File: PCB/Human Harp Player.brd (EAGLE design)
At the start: 70 x 70 mm, 41 parts, among them J1 4UCON 20404, J3 Sparkfun: PRT-00553, J4 Sparkfun: PRT-00553, J5 Sparkfun: PRT-00553, J6 Sparkfun: PRT-00553, J7 ICSP, J8 Molex: 500075-1517, Q1 MMBT2222A, Q3 STD26P3LLH6, U1 DSPIC33EP512GM604-I/PT, U2 MIC5319-3.3YD5, U3 Sparkfun: PRT-00116, X1 ABM8-16.000MHZ-B2-T

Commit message: Commit PCB Rev. 2
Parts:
- removed J6: Sparkfun: PRT-00553, SparkFun:1X06
- removed J7: ICSP, SparkFun-Connectors:1X06_NO_SILK
- removed J8: Molex: 500075-1517, x-io:500075-1517
- removed LED1: Sparkfun: COM-12903 (purple), SparkFun-LED:LED5MM
- removed Q3: STD26P3LLH6, transistor-fet:TO252
- removed R10: 10k, 0603, SparkFun:0402-RES
- removed R11: 15R, 0603, SparkFun:0402-RES
- removed S1: RS: 5MS1S102AM2QES, x-io:5MS1S102AM2QES
- removed S2: TE Connectivity: FSM4JAH, SparkFun-Electromechanical:TACTILE-PTH
- removed U$3: (no value), x-io:HUMAN_HARP_LOGO_20MM_BOTTOM
- added C12, C15, C16: 100n, 0603, SparkFun:0402-CAP
- added C13, C14: 22p, 0603, SparkFun:0402-CAP
- added J2: Unpopulated, SparkFun-Connectors:1X05
- added L1: 220u, 510mA, EATON-DRA73-221-R, rcl:PIS2816
- added LOGO1: OSHW-LOGOL, SparkFun-Aesthetics:OSHW-LOGO-L
- added Q2: IRLML6401PBF, SparkFun-DiscreteSemi:SOT23-3
- added U$2: (no value), x-io:HEDS-5600-A06
- added U4: DSPIC33EP512GM604-I/PT, x-io:TQFP44
- added U5, U6: WS2811, SparkFun-LED:LED-TRICOLOR-5050-IC
- C1: value 100n, 0603 -> 470u, 16V, Pansonic F; device SparkFun:0402-CAP -> rcl:PANASONIC_F
- C10, C8: value 100n, 0603 -> 10u, 0603
- C11: value 470u, 10V, Tant, Case E -> 10u, 0603; device rcl:SMC_E -> SparkFun:0402-CAP
- C5, C6: value 22p, 0603 -> 100n, 0603
- C9: value 10u, 0603 -> 100n, 0603
- J1: value 4UCON 20404 -> Sparkfun-PRT-00587; device x-io:JST-R/A -> SparkFun-Connectors:USB-MINIB
- J3: value Sparkfun: PRT-00553 -> Sparkfun: PRT-00116
- J4: value Sparkfun: PRT-00553 -> Unpopulated; device SparkFun-Connectors:1X05 -> SparkFun-Connectors:1X06_NO_SILK
- J5: value Sparkfun: PRT-00553 -> Sparkfun: PRT-00116; device SparkFun-Connectors:1X03 -> SparkFun-Connectors:1X05
- Q1: value MMBT2222A -> IRLML6401PBF
- R1, R6, R7: value 10k 0603 -> 4k7, 0603
- R2, R3, R4, R5, R8, R9: value 10k, 0603 -> 4k7, 0603
- U$1: device x-io:X-IO_TECHNOLOGIES_LOGO_10MM_BOTTOM -> x-io:X-IO_TECHNOLOGIES_LOGO_10MM_TOP
- U$4: value OSHW_LOGO6MM_BOTTOM -> (none); device x-io:OSHW_LOGO_6MM_BOTTOM -> x-io:HUMAN_HARP_LOGO_20MM_TOP
- U1: value DSPIC33EP512GM604-I/PT -> FT232RL; device x-io:TQFP44 -> SparkFun:SSOP28DB
- U2: value MIC5319-3.3YD5 -> BMX055; device x-io:SOT23-5 -> x-io:BMX055
- U3: value Sparkfun: PRT-00116 -> MIC5319-3.3YD5; device x-io-EAGLE-Library:X-OSC_TH -> x-io:SOT23-5
- X1: value ABM8-16.000MHZ-B2-T -> ABRACON-ABM8-16.000MHZ-B2-T
- moved J1 56.9 mm to (32.4, 66.0), turned to 180 degrees
- moved R8 45.2 mm to (63.5, 15.2), flipped to the top, turned to 180 degrees
- moved Q1 45.0 mm to (14.0, 55.9), flipped to the top, turned to 270 degrees
- moved C11 44.3 mm to (12.7, 31.1), flipped to the top, turned to 0 degrees
- moved C8 43.9 mm to (26.7, 55.9), flipped to the top, turned to 270 degrees
- moved C10 43.5 mm to (33.0, 55.9), flipped to the top
- moved R6 40.2 mm to (24.1, 54.6), flipped to the top
- moved R3 40.0 mm to (55.9, 15.2), flipped to the top, turned to 180 degrees
- moved C2 37.8 mm to (15.2, 62.2), flipped to the top, turned to 90 degrees
- moved J5 37.7 mm to (63.5, 27.9)
- moved R7 36.4 mm to (21.6, 54.6), flipped to the top
- moved J3 33.8 mm to (55.9, 27.9), turned to 270 degrees
- moved R4 33.7 mm to (55.9, 13.3), flipped to the top, turned to 180 degrees
- moved C9 33.6 mm to (26.7, 52.1), flipped to the top, turned to 270 degrees
- moved U2 31.6 mm to (37.5, 41.9), flipped to the top, turned to 0 degrees
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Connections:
- removed net AUX: J7.6, U1.25
- removed net BATTERY_LEVEL: C10.1, R6.1, R7.2, U1.19
- removed net BUTTON: S2.3, U1.26
- removed net ENCODER_VDD: J3.2, R2.2, R3.2, U1.35
- removed net IMU_INT: J4.4, U1.36
- removed net IMU_SCL: J4.3, R4.1, U1.38
- removed net IMU_SDA: J4.1, R5.1, U1.37
- removed net IMU_VDD: J4.2, R4.2, R5.2, U1.41
- removed net IN1: J6.2, U1.44, U3.1
- removed net LED: R11.1, U1.34
- removed net OUT1: J6.3, U1.43, U3.36
- removed net OUT16: J5.3, U3.21
- removed net POWER_ENABLE: U1.1
- removed net VIN: C11.+, C7.1, Q3.2, R6.2, R9.2, S1.2, U2.1, U2.3
- removed net X-OSC_ENABLE: R10.2, R8.1
- removed net X-OSC_PWR: J5.2, Q3.3, U3.20
- new net 3V3: C10.1, C12.1, C15.1, C16.2, R5.1, U3.5, U4.17, U4.28, U4.40
- new net 5V: C8.1, J3.2, Q1.3, R3.2, R4.2, U3.1, U3.3, U5.3, U5.5, U6.3, U6.5
- new net BMX055_INT: J2.4, J5.4, U2.14, U4.36
- new net BMX055_SCL: J2.3, J5.3, R8.1, U2.9, U4.38
- new net BMX055_SDA: J2.1, J5.1, R9.1, U2.11, U4.37
- new net FTDI_D+: J1.D+, U1.15
- new net FTDI_D-: J1.D-, U1.16
- new net FTDI_RX: R6.1, U1.5
- new net FTDI_SLEEP: Q2.1, R1.2, U1.12
- new net FTDI_TX: R7.1, U1.1
- new net N$6: J1.VBUS, L1.1
- new net N$8: U5.1, U6.2
- new net TEST: J4.6, U4.25
- new net VSENSORS: C5.1, C6.1, C7.2, J2.2, J5.2, R8.2, R9.2, U2.13, U2.3, U2.7, U4.41
- new net WS2811_DATA: U4.2, U5.2
- net ENCODER_A: now also R3.1, U4.32; no longer R2.1, U1.32
- net ENCODER_B: now also R4.1, U4.33; no longer R3.1, U1.33
- net GND: now also C1.-, C11.2, C12.2, C13.1, C14.1, C15.2, C16.1, C2.1, C3.1, C7.1, J1.GND, J2.5, J4.3, J5.5, R1.1, R2.1, U1.11, U1.18, U1.21, U1.25, U1.26, U1.7, U2.12, U2.17, U2.20, U2.4, U2.6, U3.2, U4.16, U4.29, U4.39, U4.6, U5.6, U6.6; no longer C1.2, C11.-, C2.2, C3.2, C7.2, J1.-, J4.5, J5.1, J6.5, J6.6, J7.3, J8.GND, LED1.K, Q1.2, R7.1, S2.1, U1.16, U1.29, U1.39, U1.6, U2.2, U3.19
- net MCLR: now also J4.1, R5.2, U4.18; no longer J7.1, R1.2, U1.18
- net N$1: now also Q2.3, R2.2; no longer R10.1
- net N$2: now also R6.2, U4.44; no longer J1.+, S1.3
- net N$3: now also C4.2, U1.17; no longer LED1.A, R11.2
- net N$4: now also C11.1, U4.7; no longer C2.1, U1.7
- net N$5: now also R7.2, U4.43; no longer Q1.3, Q3.1, R9.1
- net N$7: now also C9.1, U3.4; no longer C8.1, U2.4
- net OSC1: now also C13.2, U4.30, X1.3; no longer C6.1, U1.30, X1.1
- net OSC2: now also C14.2, U4.31, X1.1; no longer C5.1, U1.31, X1.3
- net PGEC1: now also J4.5, U4.23; no longer J7.5, U1.23
- net PGED1: now also J4.4, U4.24; no longer J7.4, U1.24
- net VBUS: now also C1.+, C2.2, C3.2, L1.2, Q1.2, Q2.2, U1.20, U1.4; no longer J6.4, J8.VBUS, S1.1
- net VDD: now also J4.2; no longer C1.1, C3.1, C4.2, C9.1, J7.2, R1.1, R8.2, U1.17, U1.28, U1.40, U2.5
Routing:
- net GND: track 138.3 -> 0.00 mm, vias 7 -> 0
- net BMX055_SDA: track 0.00 -> 75.8 mm, vias 0 -> 1
- net VSENSORS: track 0.00 -> 75.8 mm, vias 0 -> 7
- net BMX055_SCL: track 0.00 -> 72.1 mm, vias 0 -> 1
- net N$8: track 0.00 -> 68.8 mm, vias 0 -> 2
- net BMX055_INT: track 0.00 -> 68.6 mm, vias 0 -> 2
- net IN1: track 64.6 -> 0.00 mm
- net VIN: track 63.0 -> 0.00 mm
- net OUT1: track 62.4 -> 0.00 mm
- net ENCODER_B: track 12.8 -> 60.1 mm
- net 3V3: track 0.00 -> 46.4 mm, vias 0 -> 5
- net N$3: track 42.7 -> 2.17 mm
- net 5V: track 0.00 -> 38.0 mm, vias 0 -> 4
- net BUTTON: track 37.5 -> 0.00 mm
- net ENCODER_A: track 18.0 -> 52.1 mm
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- added copper zone on layer 16, net 3V3
- added copper zone on layer 16, net 5V
- added copper zone on layer 16, net VSENSORS
- removed copper zone on layer 16, net GND
- removed copper zone on layer 16, net VDD
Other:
- board size 70 x 70 mm -> 75.1 x 75 mm
- board text added: "3V3"
- board text added: "5V"
- board text added: "Human Harp Player Rev. 2"
- board text added: "TEST"
- board text removed: "AUX"
- board text removed: "Battery"
- board text removed: "DOUT"
- board text removed: "FTDI"
- board text removed: "Ground"
- board text removed: "Human Harp Player v1.0"
- board text removed: "Input 1"
- board text removed: "NeoPixels"
- board text removed: "Output 1"
- board text removed: "Output 16"
- board text removed: "PWR"
- board text removed: "RX-I"
- board text removed: "TX-O"
- board text removed: "VBUS"

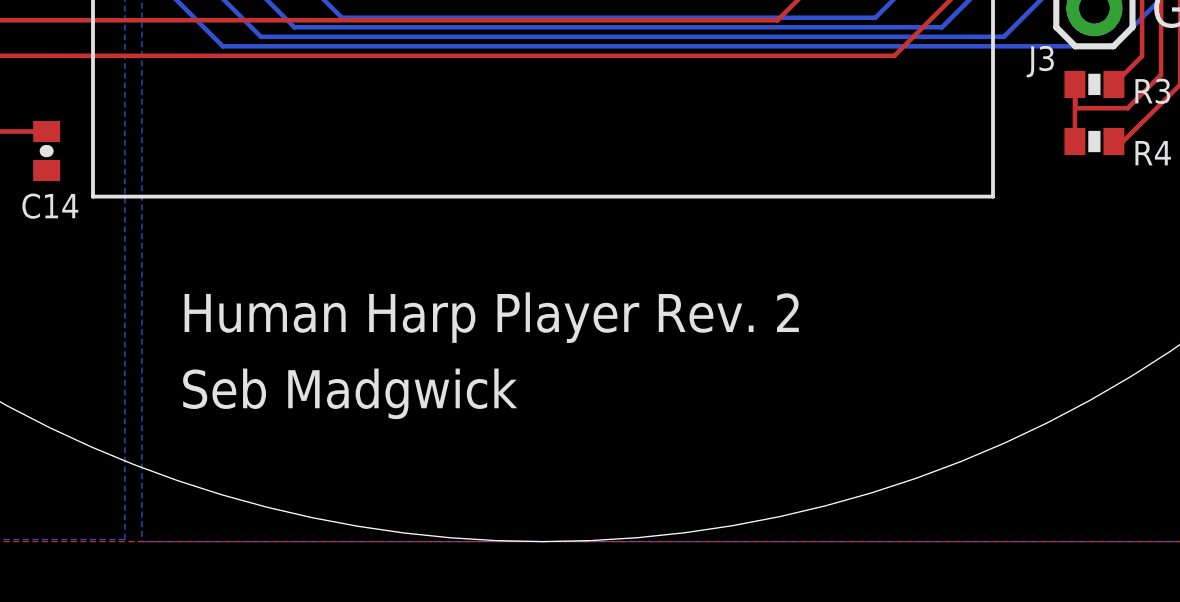
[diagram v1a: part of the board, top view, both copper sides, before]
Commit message: Add missing VDD connection to ICSP and XYZ label on PCB
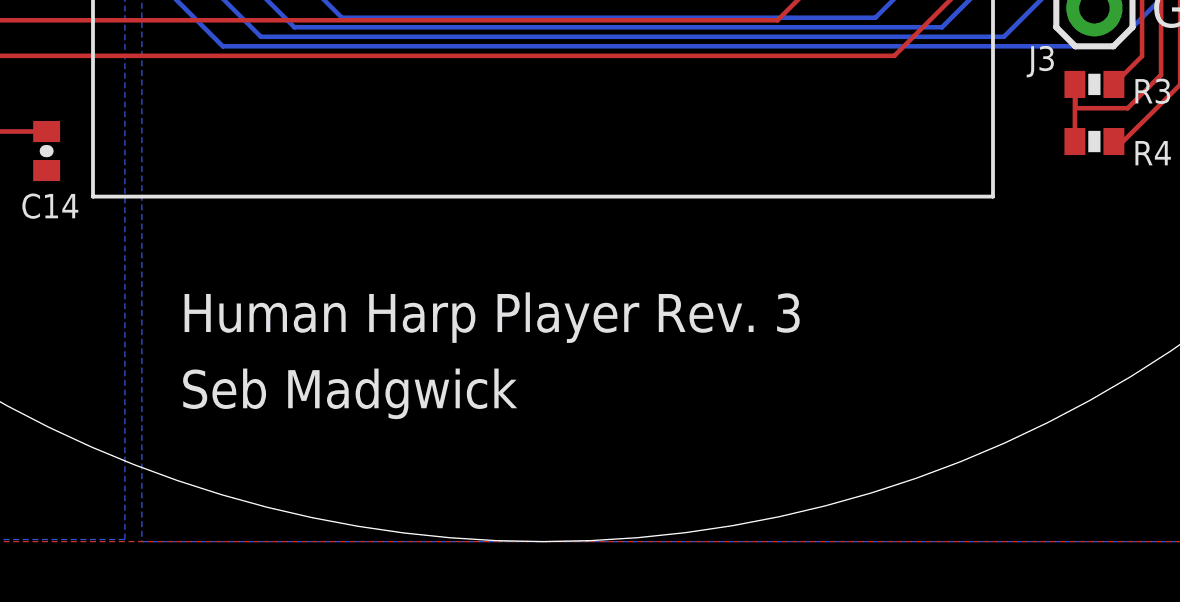
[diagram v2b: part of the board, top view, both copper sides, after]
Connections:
- removed net VDD: J4.2
- net 3V3: now also J4.2
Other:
- board text added: "Human Harp Player Rev. 3"
- board text added: "X"
- board text added: "Y"
- board text added: "Z"
- board text removed: "Human Harp Player Rev. 2"
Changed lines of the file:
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@@
 <layer number="43" name="vRestrict" color="2" fill="10" visible="no" active="yes"/>
 <layer number="44" name="Drills" color="7" fill="1" visible="no" active="yes"/>
-<layer number="45" name="Holes" color="7" fill="1" visible="no" active="yes"/>
+<layer number="45" name="Holes" color="7" fill="1" visible="yes" active="yes"/>
 <layer number="46" name="Milling" color="3" fill="1" visible="no" active="yes"/>
 <layer number="47" name="Measures" color="7" fill="1" visible="no" active="yes"/>
@@
 <text x="3.4925" y="31.4325" size="1.27" layer="122" font="vector" rot="MR180">MCLR</text>
 <text x="25.4" y="4.445" size="1.27" layer="121" font="vector">Seb Madgwick</text>
-<text x="25.4" y="6.985" size="1.27" layer="121" font="vector">Human Harp Player Rev. 2</text>
+<text x="25.4" y="6.985" size="1.27" layer="121" font="vector">Human Harp Player Rev. 3</text>
 <wire x1="37.5" y1="0" x2="0" y2="37.5" width="0" layer="20" curve="-90"/>
 <wire x1="35.56" y1="47.625" x2="39.37" y2="47.625" width="0" layer="20"/>
@@
 <circle x="14.44625" y="37.465" radius="3.971921875" width="0.4064" layer="42"/>
 <circle x="60.48375" y="37.465" radius="3.971921875" width="0.4064" layer="42"/>
+<circle x="35.56" y="40.005" radius="0.635" width="0.254" layer="122"/>
+<wire x1="36.83" y1="40.005" x2="40.005" y2="40.005" width="0.254" layer="122"/>
+<wire x1="35.56" y1="41.275" x2="35.56" y2="44.45" width="0.254" layer="122"/>
+<wire x1="35.56" y1="44.45" x2="34.925" y2="43.815" width="0.254" layer="122"/>
+<wire x1="35.56" y1="44.45" x2="36.195" y2="43.815" width="0.254" layer="122"/>
+<wire x1="40.005" y1="40.005" x2="39.37" y2="40.64" width="0.254" layer="122"/>
+<wire x1="40.005" y1="40.005" x2="39.37" y2="39.37" width="0.254" layer="122"/>
+<text x="36.195" y="44.45" size="1.27" layer="122" font="vector" rot="MR180">X</text>
+<text x="36.195" y="42.2275" size="1.27" layer="122" font="vector" rot="MR180">Z</text>
+<text x="38.4175" y="42.2275" size="1.27" layer="122" font="vector" rot="MR180">Y</text>
+<wire x1="35.2425" y1="40.3225" x2="35.8775" y2="39.6875" width="0.254" layer="122"/>
+<wire x1="35.8775" y1="40.3225" x2="35.2425" y2="39.6875" width="0.254" layer="122"/>
 </plain>
 <attributes>
@@
 <wire x1="38.115" y1="45.72" x2="33.02" y2="56.53" width="0" layer="19" extent="1-1"/>
 </signal>
-<signal name="VDD">
-<contactref element="J4" pad="2"/>
-</signal>
 <signal name="MCLR">
 <contactref element="U4" pad="18"/>
@@
 <wire x1="27.305" y1="31.75" x2="22.86" y2="27.305" width="0.6096" layer="1"/>
 <via x="22.86" y="27.305" extent="1-16" drill="0.3302"/>
+<contactref element="J4" pad="2"/>
 </signal>
 <signal name="N$1">
